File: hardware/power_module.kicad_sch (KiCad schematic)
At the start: 11 parts, among them U10 LM1117-3.3, U8 LM1117-3.3, U9 LM1117-3.3

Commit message: Refactor
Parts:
- U10, U8, U9: symbol Regulator_Linear:LM1117-3.3 -> Regulator_Linear:LM1117MP-3.3
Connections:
- net 3V3_SYS renamed +3V3
- net VO_POT1: no longer names the net of C26.1, F1.2, U9.2 (VO)
- net VO_POT2: no longer names the net of C28.1, F2.2, U10.2 (VO)
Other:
- moved on the sheet: F1, F2

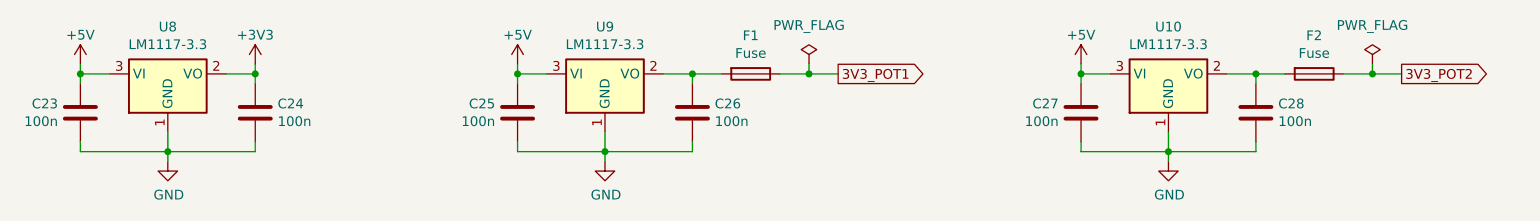
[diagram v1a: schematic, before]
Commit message: Adjust component values
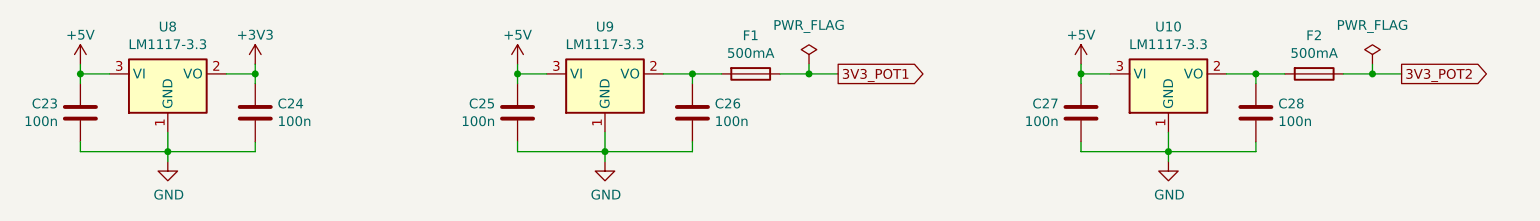
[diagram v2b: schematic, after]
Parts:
- F1, F2: value Fuse -> 500mA
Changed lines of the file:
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@@
   (title_block
     (title "Power for Potentiometers")
-    (date "2023-04-22")
+    (date "2023-06-30")
     (rev "2.0")
     (company "S. Sambor")
@@
       (effects (font (size 1.27 1.27)))
     )
-    (property "Value" "Fuse" (at 151.13 96.3676 90)
+    (property "Value" "500mA" (at 151.13 96.3676 90)
       (effects (font (size 1.27 1.27)))
     )
@@
       (effects (font (size 1.27 1.27)))
     )
-    (property "Value" "Fuse" (at 224.79 96.3676 90)
-      (effects (font (size 1.27 1.27)))
-    )
+    (property "Value" "500mA" (at 224.79 96.3676 90)
+      (effects (font (size 1.27 1.27)))
+    )
